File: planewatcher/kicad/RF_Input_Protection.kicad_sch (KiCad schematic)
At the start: 2 parts

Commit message: work on board layout
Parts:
- renumbered D2 to D3, L1 to L12
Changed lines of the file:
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@@
 		(dnp no)
 		(fields_autoplaced yes)
-		(property "Reference" "D2"
+		(property "Reference" "D3"
 			(at 142.24 96.5199 90)
 			(show_name no)
@@
 			(project "planewatcher"
 				(path "/7a4a4324-e8b8-4d06-b75a-28095d4e9f10/688449b3-e085-4d3d-9010-5bd7bcac8461"
-					(reference "D2")
+					(reference "D3")
 					(unit 1)
 				)
@@
 		(dnp no)
 		(fields_autoplaced yes)
-		(property "Reference" "L1"
+		(property "Reference" "L12"
 			(at 132.08 96.5199 0)
 			(show_name no)
@@
 			(project "planewatcher"
 				(path "/7a4a4324-e8b8-4d06-b75a-28095d4e9f10/688449b3-e085-4d3d-9010-5bd7bcac8461"
-					(reference "L1")
+					(reference "L12")
 					(unit 1)
 				)
@@
 		(dnp no)
 		(fields_autoplaced yes)
-		(property "Reference" "#PWR018"
+		(property "Reference" "#PWR0108"
 			(at 135.89 107.95 0)
 			(hide yes)
@@
 			(project "planewatcher"
 				(path "/7a4a4324-e8b8-4d06-b75a-28095d4e9f10/688449b3-e085-4d3d-9010-5bd7bcac8461"
-					(reference "#PWR018")
+					(reference "#PWR0108")
 					(unit 1)
 				)

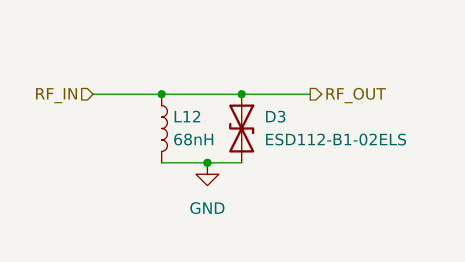
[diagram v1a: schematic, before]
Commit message: address & fix ERC errors/warnings
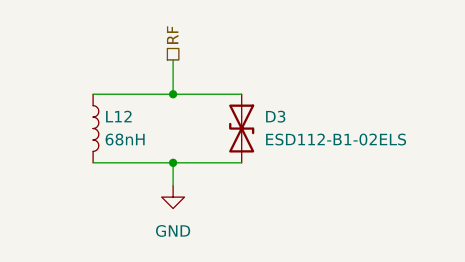
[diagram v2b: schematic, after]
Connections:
- net RF_IN renamed RF
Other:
- moved on the sheet: L12
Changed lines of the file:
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@@
 	)
 	(junction
-		(at 135.89 101.6)
+		(at 132.08 93.98)
 		(diameter 0)
 		(color 0 0 0 0)
 	)
 	(junction
-		(at 139.7 93.98)
+		(at 132.08 101.6)
 		(diameter 0)
 		(color 0 0 0 0)
 	)
-	(junction
-		(at 130.81 93.98)
-		(diameter 0)
-		(color 0 0 0 0)
-	)
-	(wire
-		(pts
-			(xy 135.89 101.6) (xy 139.7 101.6)
-		)
-		(stroke
-			(width 0)
-			(type default)
-		)
-	)
-	(wire
-		(pts
-			(xy 123.19 93.98) (xy 130.81 93.98)
-		)
-		(stroke
-			(width 0)
-			(type default)
-		)
-	)
-	(wire
-		(pts
-			(xy 130.81 101.6) (xy 135.89 101.6)
-		)
-		(stroke
-			(width 0)
-			(type default)
-		)
-	)
-	(wire
-		(pts
-			(xy 139.7 93.98) (xy 147.32 93.98)
-		)
-		(stroke
-			(width 0)
-			(type default)
-		)
-	)
-	(wire
-		(pts
-			(xy 130.81 93.98) (xy 139.7 93.98)
-		)
-		(stroke
-			(width 0)
-			(type default)
-		)
-	)
-	(hierarchical_label "RF_OUT"
-		(shape output)
-		(at 147.32 93.98 0)
+	(wire
+		(pts
+			(xy 132.08 101.6) (xy 139.7 101.6)
+		)
+		(stroke
+			(width 0)
+			(type default)
+		)
+	)
+	(wire
+		(pts
+			(xy 132.08 93.98) (xy 139.7 93.98)
+		)
+		(stroke
+			(width 0)
+			(type default)
+		)
+	)
+	(wire
+		(pts
+			(xy 132.08 90.17) (xy 132.08 93.98)
+		)
+		(stroke
+			(width 0)
+			(type default)
+		)
+	)
+	(wire
+		(pts
+			(xy 132.08 104.14) (xy 132.08 101.6)
+		)
+		(stroke
+			(width 0)
+			(type default)
+		)
+	)
+	(wire
+		(pts
+			(xy 123.19 101.6) (xy 132.08 101.6)
+		)
+		(stroke
+			(width 0)
+			(type default)
+		)
+	)
+	(wire
+		(pts
+			(xy 123.19 93.98) (xy 132.08 93.98)
+		)
+		(stroke
+			(width 0)
+			(type default)
+		)
+	)
+	(hierarchical_label "RF"
+		(shape passive)
+		(at 132.08 90.17 90)
 		(effects
 			(font
@@
 			)
 			(justify left)
-		)
-	)
-	(hierarchical_label "RF_IN"
-		(shape input)
-		(at 123.19 93.98 180)
-		(effects
-			(font
-				(size 1.27 1.27)
-			)
-			(justify right)
 		)
 	)
@@
 	(symbol
 		(lib_id "Device:L")
-		(at 130.81 97.79 0)
+		(at 123.19 97.79 0)
 		(unit 1)
 		(body_style 1)
@@
 		(fields_autoplaced yes)
 		(property "Reference" "L12"
-			(at 132.08 96.5199 0)
+			(at 124.46 96.5199 0)
 			(show_name no)
 			(do_not_autoplace no)
@@
 		)
 		(property "Value" "68nH"
-			(at 132.08 99.0599 0)
+			(at 124.46 99.0599 0)
 			(show_name no)
 			(do_not_autoplace no)
@@
 		)
 		(property "Footprint" "planewatcher:L_Coilcraft_0402DC_1005Metric"
-			(at 130.81 97.79 0)
+			(at 123.19 97.79 0)
 			(hide yes)
 			(show_name no)
@@
 		)
 		(property "Datasheet" "https://www.coilcraft.com/getmedia/b3553702-9a56-4386-b513-fcddf8709240/0402dc.pdf"
-			(at 130.81 97.79 0)
+			(at 123.19 97.79 0)
 			(hide yes)
 			(show_name no)
@@
 		)
 		(property "Description" "Inductor"
-			(at 130.81 97.79 0)
+			(at 123.19 97.79 0)
 			(hide yes)
 			(show_name no)
@@
 		)
 		(property "Purpose" "RF choke/shunt inductor to ground. Provides DC/static bleed and input matching/filtering behaviour at 1090 MHz."
-			(at 130.81 97.79 0)
+			(at 123.19 97.79 0)
 			(hide yes)
 			(show_name no)
@@
 		)
 		(property "Notes" ""
-			(at 130.81 97.79 0)
+			(at 123.19 97.79 0)
 			(hide yes)
 			(show_name no)
@@
 	(symbol
 		(lib_id "power:GND")
-		(at 135.89 101.6 0)
+		(at 132.08 104.14 0)
 		(unit 1)
 		(body_style 1)
@@
 		(fields_autoplaced yes)
 		(property "Reference" "#PWR0108"
-			(at 135.89 107.95 0)
+			(at 132.08 110.49 0)
 			(hide yes)
 			(show_name no)
@@
 		)
 		(property "Value" "GND"
-			(at 135.89 106.68 0)
+			(at 132.08 109.22 0)
 			(show_name no)
 			(do_not_autoplace no)
@@
 		)
 		(property "Footprint" ""
-			(at 135.89 101.6 0)
+			(at 132.08 104.14 0)
 			(hide yes)
 			(show_name no)
@@
 		)
 		(property "Datasheet" ""
-			(at 135.89 101.6 0)
+			(at 132.08 104.14 0)
 			(hide yes)
 			(show_name no)
@@
 		)
 		(property "Description" "Power symbol creates a global label with name \"GND\" , ground"
-			(at 135.89 101.6 0)
-			(hide yes)
-			(show_name no)
+			(at 132.08 104.14 0)
+			(hide yes)
+			(show_name no)

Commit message: updates before fab
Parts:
- D3: value ESD112-B1-02ELS -> ESD103-B1-02EL; Suggested Part (none) -> Infineon ESD103B102ELE6327XTMA1
- L12: Purpose RF choke/shunt inductor to ground. Provides DC/static bleed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 -> RF choke/shunt inductor to ground; provides DC/static bleed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; Suggested Part (none) -> Coilcraft 0402DC-68NXJRW
